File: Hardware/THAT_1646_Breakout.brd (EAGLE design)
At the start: 45.7 x 20.3 mm, 29 parts, among them IC1 THAT1646, J1 1x4, J2 SN, J3 CHASSIS, J4 TN, J5 RN, J6 OUTPUT, J7 T, J8 R

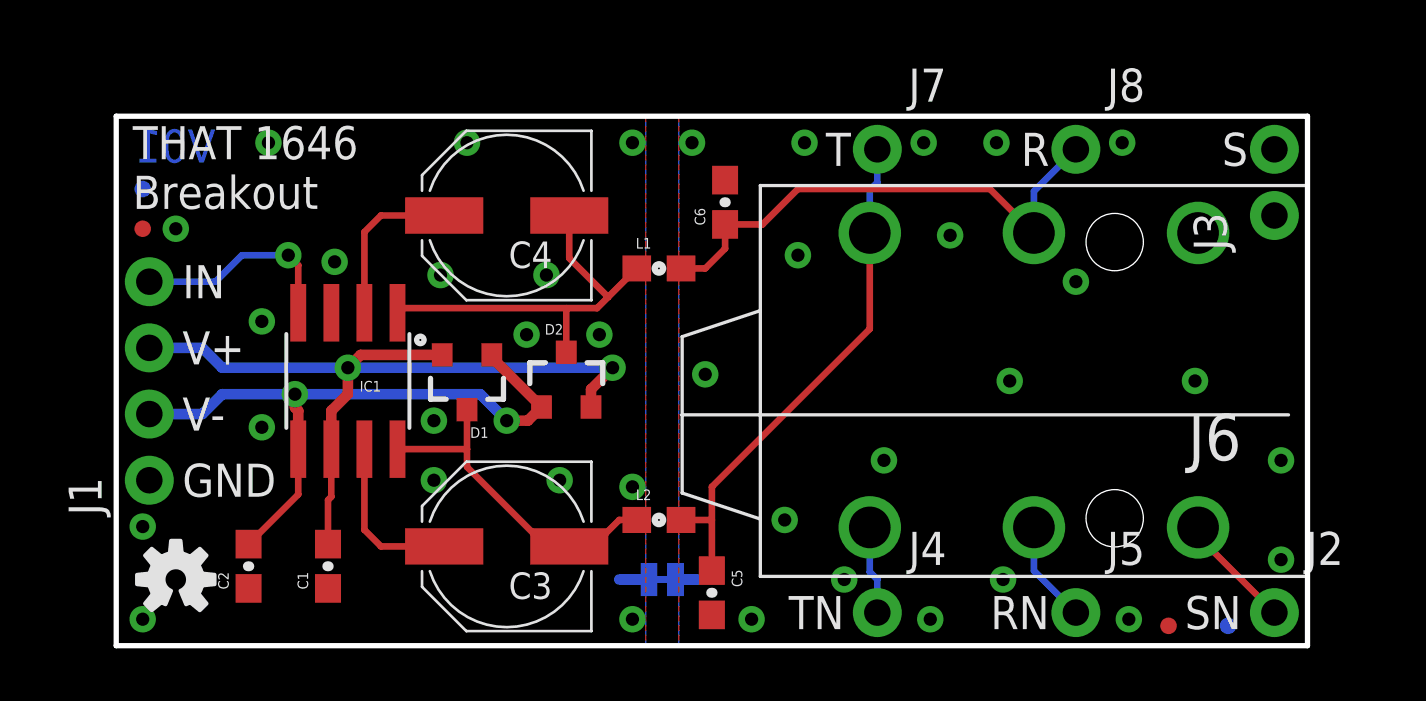
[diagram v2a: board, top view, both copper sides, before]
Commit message: Updates after group review.
-Chassis ground pad moved away from selective solder runout.
-Version numbers fixed.
-Top/bottom fiducials co-located.
-Flame oriented to match text.
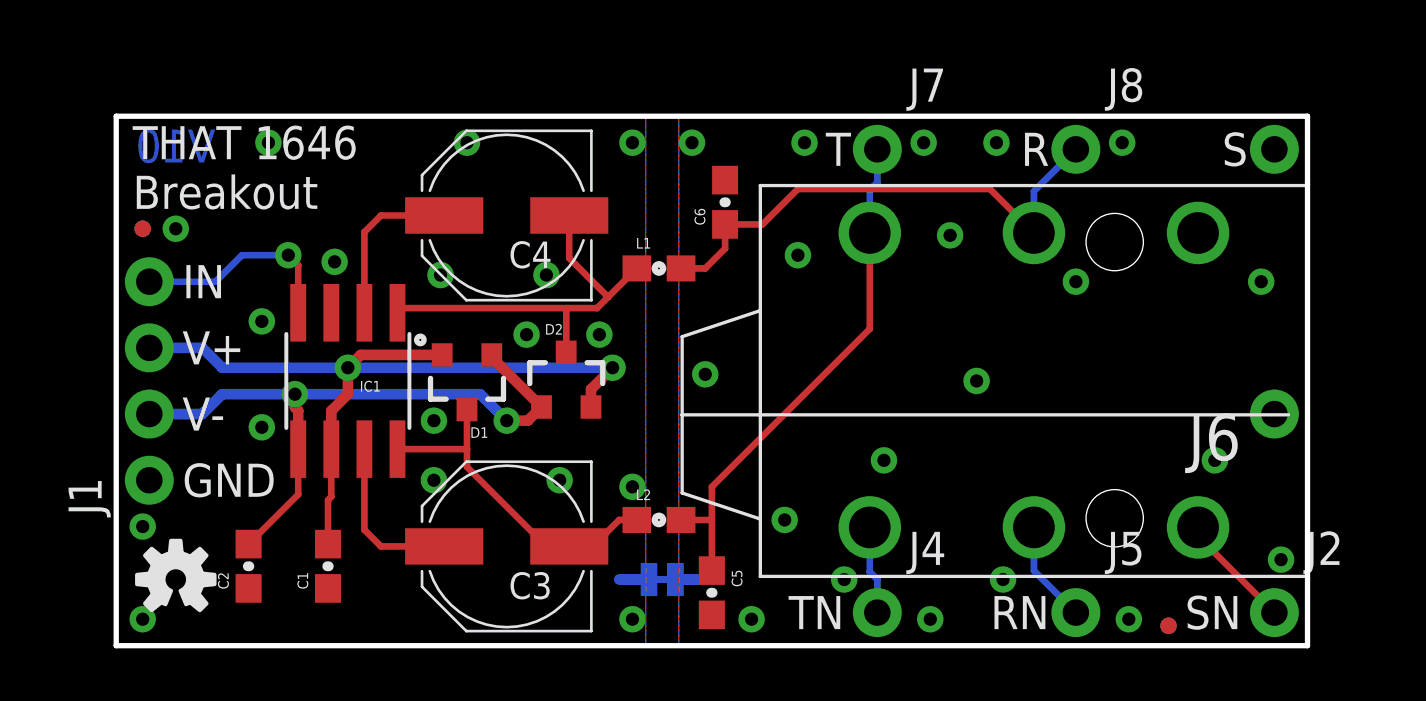
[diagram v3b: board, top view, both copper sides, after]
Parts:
- added J9: Chassis, SparkFun-Connectors:1X01_NO_SILK
- J3: value CHASSIS -> S; device SparkFun-Connectors:1X02_NO_SILK -> SparkFun-Connectors:1X01_NO_SILK
- moved LOGO4 3.82 mm to (38.4, 7.24), turned to 0 degrees
- moved J3 2.54 mm to (44.5, 19.1), flipped to the bottom, turned to 0 degrees
- moved FD2 2.29 mm to (40.4, 0.76)
- moved FD1 1.52 mm to (1.02, 16.0)
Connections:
- net GND-ISO: now also J9.1; no longer J3.2
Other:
- board text added: "V10"
- board text removed: "V01"
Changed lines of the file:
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@@
 <layer number="23" name="tOrigins" color="15" fill="1" visible="yes" active="yes"/>
 <layer number="24" name="bOrigins" color="15" fill="1" visible="yes" active="yes"/>
-<layer number="25" name="tNames" color="7" fill="1" visible="no" active="yes"/>
+<layer number="25" name="tNames" color="7" fill="1" visible="yes" active="yes"/>
 <layer number="26" name="bNames" color="7" fill="1" visible="no" active="yes"/>
 <layer number="27" name="tValues" color="7" fill="1" visible="no" active="yes"/>
@@
 <layer number="43" name="vRestrict" color="2" fill="10" visible="no" active="yes"/>
 <layer number="44" name="Drills" color="7" fill="1" visible="no" active="yes"/>
-<layer number="45" name="Holes" color="7" fill="1" visible="yes" active="yes"/>
+<layer number="45" name="Holes" color="7" fill="1" visible="no" active="yes"/>
 <layer number="46" name="Milling" color="3" fill="1" visible="no" active="yes"/>
-<layer number="47" name="Measures" color="7" fill="1" visible="yes" active="yes"/>
+<layer number="47" name="Measures" color="7" fill="1" visible="no" active="yes"/>
 <layer number="48" name="Document" color="7" fill="1" visible="no" active="yes"/>
 <layer number="49" name="Reference" color="7" fill="1" visible="no" active="yes"/>
 <layer number="50" name="dxf" color="7" fill="1" visible="no" active="no"/>
-<layer number="51" name="tDocu" color="6" fill="1" visible="yes" active="yes"/>
+<layer number="51" name="tDocu" color="6" fill="1" visible="no" active="yes"/>
 <layer number="52" name="bDocu" color="7" fill="1" visible="no" active="yes"/>
 <layer number="53" name="tGND_GNDA" color="7" fill="9" visible="no" active="no"/>
@@
 <text x="2.54" y="13.97" size="1.27" layer="21" font="vector" ratio="15" rot="R180" align="center-right">IN</text>
 <text x="46.99" y="-20.32" size="1.778" layer="51" font="vector" ratio="15">Byron Jacquot</text>
-<text x="3.81" y="18.542" size="1.27" layer="16" font="vector" ratio="20" rot="MR0">V01</text>
+<text x="3.81" y="18.542" size="1.27" layer="16" font="vector" ratio="20" rot="MR0">V10</text>
 <text x="23.876" y="10.668" size="1.27" layer="22" font="vector" ratio="15" rot="MR0" align="center">THAT 1646
 OutSmarts
@@
 isolate chassis
 and circuit grounds</text>
-<text x="44.45" y="15.494" size="1.27" layer="22" font="vector" ratio="15" rot="MR90" align="center-right">Chassis</text>
+<text x="44.45" y="9.906" size="1.27" layer="22" font="vector" ratio="15" rot="MR270" align="center-right">Chassis</text>
 <dimension x1="0" y1="0" x2="0" y2="20.32" x3="-5.842" y3="10.16" textsize="1.778" textratio="15" layer="47" unit="inch"/>
 <dimension x1="0" y1="0" x2="45.72" y2="0" x3="22.86" y3="-5.842" textsize="1.778" textratio="15" layer="47" unit="inch"/>
@@
 <attribute name="PROD_ID" value="CONN-09696" x="1.27" y="6.35" size="1.778" layer="27" font="vector" ratio="15" rot="R90" display="off"/>
 </element>
-<element name="J3" library="SparkFun-Connectors" package="1X02_NO_SILK" value="CHASSIS" x="44.45" y="16.51" rot="R90"/>
 <element name="FD3" library="SparkFun-Aesthetics" package="MICRO-FIDUCIAL" value="FIDUCIALUFIDUCIAL" x="1.016" y="16.002"/>
 <element name="FD4" library="SparkFun-Aesthetics" package="MICRO-FIDUCIAL" value="FIDUCIALUFIDUCIAL" x="40.386" y="0.762"/>
@@
 <element name="J4" library="SparkFun-Connectors" package="1X01_NO_SILK" value="TN" x="29.21" y="1.27"/>
 <element name="J5" library="SparkFun-Connectors" package="1X01_NO_SILK" value="RN" x="36.83" y="1.27"/>
-<element name="LOGO4" library="SparkFun-Aesthetics" package="SFE_LOGO_FLAME_.2" value="SFE_LOGO_FLAME.2_INCH" x="34.798" y="8.636" rot="MR90"/>
-<element name="FD1" library="SparkFun-Aesthetics" package="MICRO-FIDUCIAL" value="FIDUCIALUFIDUCIAL" x="1.016" y="17.526" rot="MR0"/>
-<element name="FD2" library="SparkFun-Aesthetics" package="MICRO-FIDUCIAL" value="FIDUCIALUFIDUCIAL" x="42.672" y="0.762" rot="MR0"/>
+<element name="LOGO4" library="SparkFun-Aesthetics" package="SFE_LOGO_FLAME_.2" value="SFE_LOGO_FLAME.2_INCH" x="38.354" y="7.239" rot="MR0"/>
+<element name="FD1" library="SparkFun-Aesthetics" package="MICRO-FIDUCIAL" value="FIDUCIALUFIDUCIAL" x="1.016" y="16.002" rot="MR0"/>
+<element name="FD2" library="SparkFun-Aesthetics" package="MICRO-FIDUCIAL" value="FIDUCIALUFIDUCIAL" x="40.386" y="0.762" rot="MR0"/>
 <element name="C3" library="that-ics" package="PANASONIC_D" value="10uf NP" x="14.986" y="3.81" rot="R180">
 <attribute name="DK_PN" value="PCE4294TR-ND" x="14.986" y="3.81" size="1.778" layer="27" font="vector" ratio="15" rot="R180" display="off"/>
@@
 <element name="J7" library="SparkFun-Connectors" package="1X01_NO_SILK" value="T" x="29.21" y="19.05"/>
 <element name="J8" library="SparkFun-Connectors" package="1X01_NO_SILK" value="R" x="36.83" y="19.05"/>
+<element name="J9" library="SparkFun-Connectors" package="1X01_NO_SILK" value="Chassis" x="44.45" y="8.89" rot="MR0"/>
+<element name="J3" library="SparkFun-Connectors" package="1X01_NO_SILK" value="S" x="44.45" y="19.05" rot="MR0"/>
 </elements>
 <signals>
@@
 <vertex x="21.59" y="0"/>
 </polygon>
-<contactref element="J3" pad="1"/>
-<contactref element="J3" pad="2"/>
 <wire x1="21.463" y1="2.54" x2="22.606" y2="2.54" width="0.4064" layer="16"/>
 <via x="22.098" y="19.304" extent="1-16" drill="0.508"/>
 <via x="26.416" y="19.304" extent="1-16" drill="0.508"/>
 <via x="36.83" y="13.97" extent="1-16" drill="0.508"/>
-<via x="44.704" y="7.112" extent="1-16" drill="0.508"/>
-<via x="34.29" y="10.16" extent="1-16" drill="0.508"/>
+<via x="42.164" y="7.112" extent="1-16" drill="0.508"/>
+<via x="33.02" y="10.16" extent="1-16" drill="0.508"/>
 <via x="29.464" y="7.112" extent="1-16" drill="0.508"/>
 <via x="31.242" y="1.016" extent="1-16" drill="0.508"/>
@@
 <via x="38.608" y="19.304" extent="1-16" drill="0.508"/>
 <via x="24.384" y="1.016" extent="1-16" drill="0.508"/>
-<via x="41.402" y="10.16" extent="1-16" drill="0.508"/>
+<via x="43.942" y="13.97" extent="1-16" drill="0.508"/>
+<contactref element="J9" pad="1"/>
+<contactref element="J3" pad="1"/>
 </signal>
 <signal name="N$8">

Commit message: Engineering checklist updates.
Found too narrow silk in some packages.
Moves a couple vias out from under silk text.
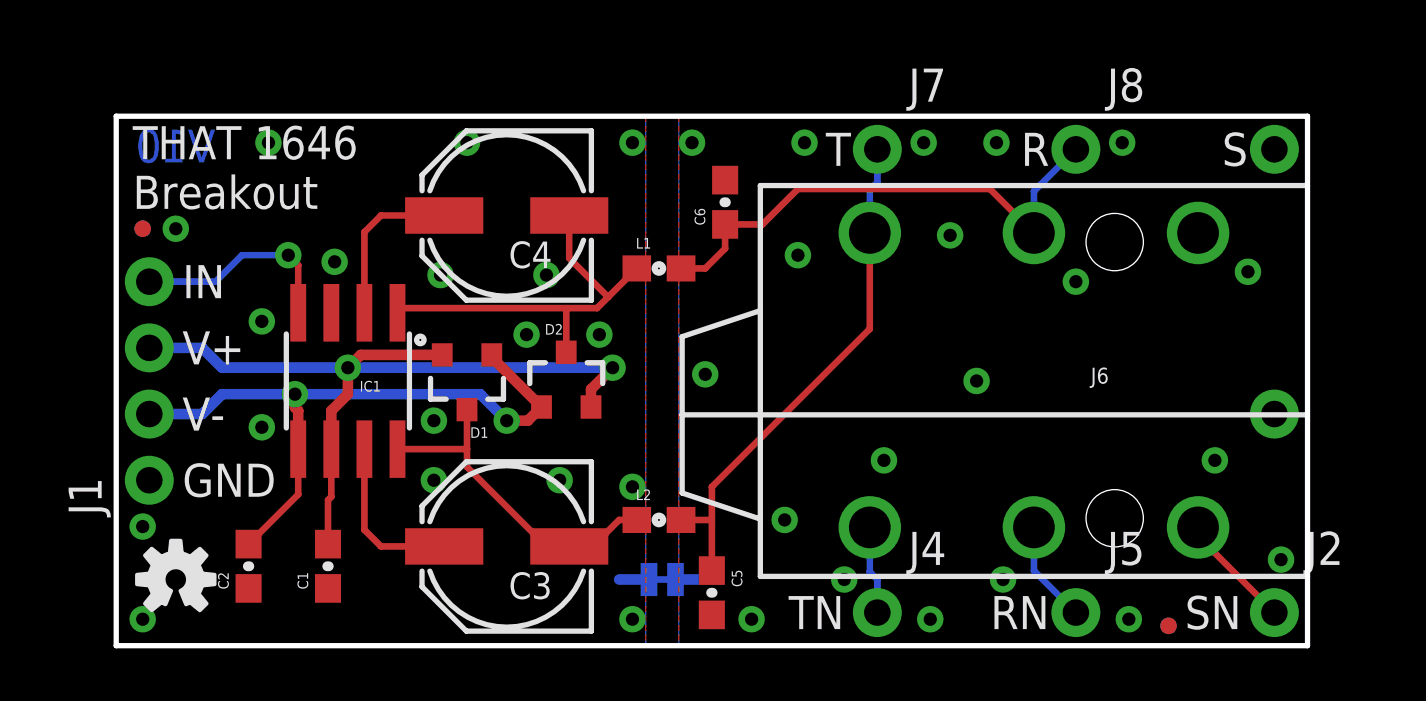
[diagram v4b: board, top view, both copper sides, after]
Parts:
- J6: device SparkFun-Connectors:AUDIO-JACK-.25-INCH-HORIZ-PTH -> SparkFun-Connectors:AUDIO_JACK_0.25"_TRS_PTH_RA
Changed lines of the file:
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@@
 <grid distance="0.05" unitdist="inch" unit="inch" style="lines" multiple="1" display="yes" altdistance="0.005" altunitdist="inch" altunit="inch"/>
 <layers>
-<layer number="1" name="Top" color="4" fill="1" visible="yes" active="yes"/>
+<layer number="1" name="Top" color="4" fill="1" visible="no" active="yes"/>
 <layer number="2" name="Route2" color="1" fill="3" visible="no" active="no"/>
 <layer number="3" name="Route3" color="4" fill="3" visible="no" active="no"/>
@@
 <layer number="14" name="Route14" color="1" fill="6" visible="no" active="no"/>
 <layer number="15" name="Route15" color="4" fill="6" visible="no" active="no"/>
-<layer number="16" name="Bottom" color="1" fill="1" visible="yes" active="yes"/>
-<layer number="17" name="Pads" color="2" fill="1" visible="yes" active="yes"/>
+<layer number="16" name="Bottom" color="1" fill="1" visible="no" active="yes"/>
+<layer number="17" name="Pads" color="2" fill="1" visible="no" active="yes"/>
 <layer number="18" name="Vias" color="2" fill="1" visible="yes" active="yes"/>
 <layer number="19" name="Unrouted" color="6" fill="1" visible="yes" active="yes"/>
@@
 <layer number="25" name="tNames" color="7" fill="1" visible="yes" active="yes"/>
 <layer number="26" name="bNames" color="7" fill="1" visible="no" active="yes"/>
-<layer number="27" name="tValues" color="7" fill="1" visible="no" active="yes"/>
+<layer number="27" name="tValues" color="7" fill="1" visible="yes" active="yes"/>
 <layer number="28" name="bValues" color="7" fill="1" visible="no" active="yes"/>
 <layer number="29" name="tStop" color="7" fill="3" visible="no" active="yes"/>
@@
 <layer number="37" name="tTest" color="7" fill="1" visible="no" active="yes"/>
 <layer number="38" name="bTest" color="7" fill="1" visible="no" active="yes"/>
-<layer number="39" name="tKeepout" color="4" fill="11" visible="no" active="yes"/>
-<layer number="40" name="bKeepout" color="1" fill="11" visible="no" active="yes"/>
+<layer number="39" name="tKeepout" color="4" fill="11" visible="yes" active="yes"/>
+<layer number="40" name="bKeepout" color="1" fill="11" visible="yes" active="yes"/>
 <layer number="41" name="tRestrict" color="4" fill="10" visible="no" active="yes"/>
 <layer number="42" name="bRestrict" color="1" fill="10" visible="no" active="yes"/>
 <layer number="43" name="vRestrict" color="2" fill="10" visible="no" active="yes"/>
 <layer number="44" name="Drills" color="7" fill="1" visible="no" active="yes"/>
-<layer number="45" name="Holes" color="7" fill="1" visible="no" active="yes"/>
+<layer number="45" name="Holes" color="7" fill="1" visible="yes" active="yes"/>
 <layer number="46" name="Milling" color="3" fill="1" visible="no" active="yes"/>
-<layer number="47" name="Measures" color="7" fill="1" visible="no" active="yes"/>
+<layer number="47" name="Measures" color="7" fill="1" visible="yes" active="yes"/>
 <layer number="48" name="Document" color="7" fill="1" visible="no" active="yes"/>
 <layer number="49" name="Reference" color="7" fill="1" visible="no" active="yes"/>
 <layer number="50" name="dxf" color="7" fill="1" visible="no" active="no"/>
-<layer number="51" name="tDocu" color="6" fill="1" visible="no" active="yes"/>
+<layer number="51" name="tDocu" color="6" fill="1" visible="yes" active="yes"/>
 <layer number="52" name="bDocu" color="7" fill="1" visible="no" active="yes"/>
 <layer number="53" name="tGND_GNDA" color="7" fill="9" visible="no" active="no"/>
@@
 <attribute name="PROD_ID" value="IC-13473" x="8.89" y="10.16" size="1.778" layer="27" rot="R180" display="off"/>
 </element>
-<element name="J6" library="SparkFun-Connectors" package="AUDIO-JACK-.25-INCH-HORIZ-PTH" value="OUTPUT" x="45.72" y="8.89" rot="R180">
+<element name="J6" library="SparkFun-Connectors" package="AUDIO_JACK_0.25&quot;_TRS_PTH_RA" value="OUTPUT" x="45.72" y="8.89" rot="R180">
 <attribute name="PROD_ID" value="CONN-12339" x="45.72" y="8.89" size="1.778" layer="27" rot="R180" display="off"/>
 <attribute name="SF_ID" value="COM-11144" x="45.72" y="8.89" size="1.778" layer="27" rot="R180" display="off"/>
@@
 <via x="38.608" y="19.304" extent="1-16" drill="0.508"/>
 <via x="24.384" y="1.016" extent="1-16" drill="0.508"/>
-<via x="43.942" y="13.97" extent="1-16" drill="0.508"/>
+<via x="43.434" y="14.351" extent="1-16" drill="0.508"/>
 <contactref element="J9" pad="1"/>
 <contactref element="J3" pad="1"/>
